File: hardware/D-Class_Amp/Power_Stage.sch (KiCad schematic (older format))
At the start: 18 parts, among them Q501 PHP23NQ11T, Q502 PHP23NQ11T, Q503 PHP23NQ11T, Q504 PHP23NQ11T, U502 IR21834, U503 IR21834

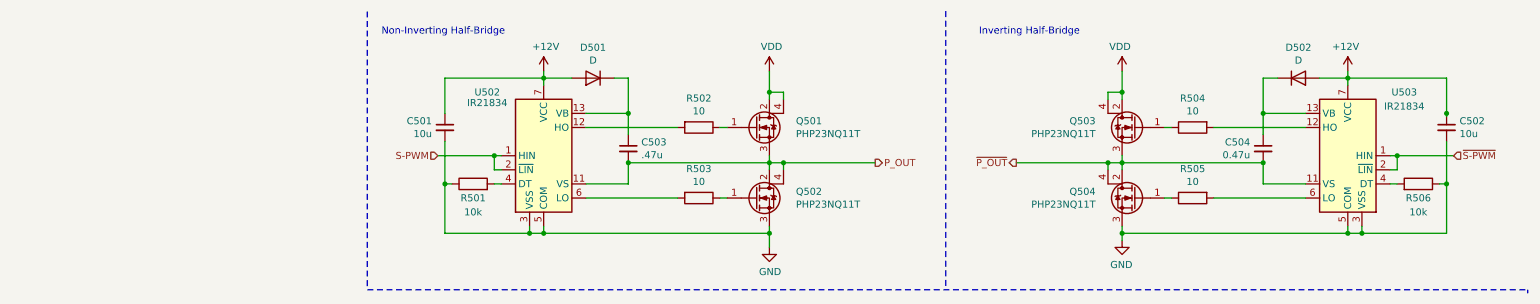
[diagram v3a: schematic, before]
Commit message: updated fet footprints, and added power stage test points
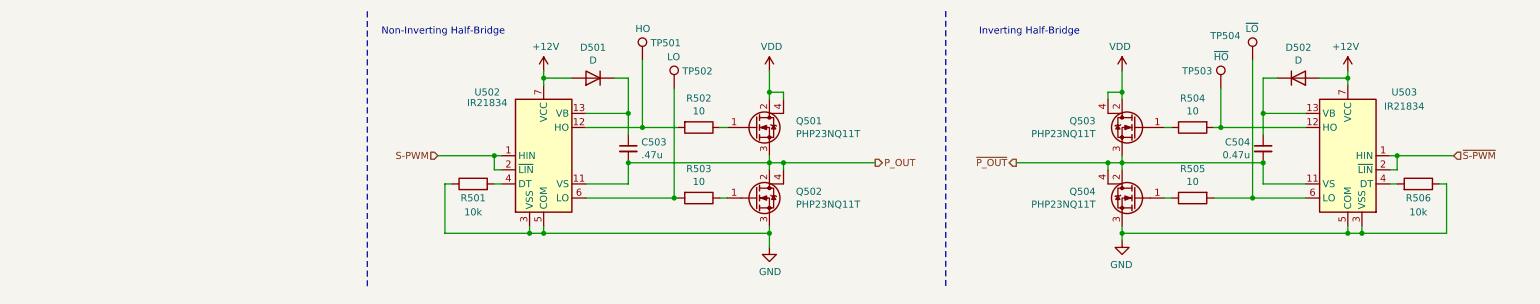
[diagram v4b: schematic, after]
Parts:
- removed C501, C502: 10u, Capacitor_SMD:C_0805_2012Metric_Pad1.18x1.45mm_HandSolder, symbol Device:C_Small
- added TP501: HO, TestPoint:TestPoint_THTPad_D2.0mm_Drill1.0mm, symbol Connector:TestPoint
- added TP502: LO, TestPoint:TestPoint_THTPad_D2.0mm_Drill1.0mm, symbol Connector:TestPoint
- added TP503: ~HO, TestPoint:TestPoint_THTPad_D2.0mm_Drill1.0mm, symbol Connector:TestPoint
- added TP504: ~LO, TestPoint:TestPoint_THTPad_D2.0mm_Drill1.0mm, symbol Connector:TestPoint
- Q502, Q503, Q504: footprint Package_TO_SOT_THT:TO-251-3-1EP_Horizontal_TabD -> Package_TO_SOT_THT:TO-251-3-1EP_Horizontal_TabDown
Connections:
- net at R502.2, U502.12 (HO): now also TP501.1
- net at R503.2, U502.6 (LO): now also TP502.1
- net at R504.2, U503.12 (HO): now also TP503.1
- net at R505.2, U503.6 (LO): now also TP504.1
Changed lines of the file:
@@
 Connection ~ 5950 1550
 Wire Wire Line
-	4550 1300 5200 1300
-Wire Wire Line
-	4550 1800 5200 1800
+	4550 1300 4950 1300
 Wire Wire Line
 	5850 1550 4850 1550
@@
 $EndComp
 $Comp
-L Device:Q_NMOS_GDSD Q502
-U 1 1 6104F394
-P 5750 1800
-F 0 "Q502" H 6038 1846 50  0000 L CNN
-F 1 "PHP23NQ11T" H 6038 1755 50  0000 L CNN
-F 2 "Package_TO_SOT_THT:TO-251-3-1EP_Horizontal_TabD" H 5950 1900 50  0001 C CNN
-F 3 "https://assets.nexperia.com/documents/data-sheet/PHP23NQ11T.pdf" H 5750 1800 50  0001 C CNN
-	1    5750 1800
-	1    0    0    -1
-$EndComp
-$Comp
 L Device:Q_NMOS_GDSD Q501
 U 1 1 6104F024
@@
 $EndComp
 $Comp
-L Device:Q_NMOS_GDSD Q503
-U 1 1 610F221C
-P 8450 1300
-F 0 "Q503" H 8738 1346 50  0000 L CNN
-F 1 "PHP23NQ11T" H 8738 1255 50  0000 L CNN
-F 2 "Package_TO_SOT_THT:TO-251-3-1EP_Horizontal_TabD" H 8650 1400 50  0001 C CNN
-F 3 "https://assets.nexperia.com/documents/data-sheet/PHP23NQ11T.pdf" H 8450 1300 50  0001 C CNN
-	1    8450 1300
-	-1   0    0    -1
-$EndComp
-$Comp
-L Device:Q_NMOS_GDSD Q504
-U 1 1 610F2226
-P 8450 1800
-F 0 "Q504" H 8738 1846 50  0000 L CNN
-F 1 "PHP23NQ11T" H 8738 1755 50  0000 L CNN
-F 2 "Package_TO_SOT_THT:TO-251-3-1EP_Horizontal_TabD" H 8650 1900 50  0001 C CNN
-F 3 "https://assets.nexperia.com/documents/data-sheet/PHP23NQ11T.pdf" H 8450 1800 50  0001 C CNN
-	1    8450 1800
-	-1   0    0    -1
-$EndComp
-$Comp
 L Driver_FET:IR21834 U503
 U 1 1 610F2212
@@
 	8350 1550 9350 1550
 Wire Wire Line
-	9650 1800 9000 1800
-Wire Wire Line
-	9650 1300 9000 1300
+	9650 1800 9275 1800
+Wire Wire Line
+	9650 1300 9050 1300
 Connection ~ 8250 1550
 Wire Wire Line
@@
 	8350 1100 8350 1050
 Connection ~ 8350 1550
-Wire Wire Line
-	8350 1550 8350 1500
 Wire Wire Line
 	8350 1550 8350 1600
@@
 $EndComp
 $Comp
-L Device:C_Small C501
-U 1 1 61139FFD
-P 3550 1300
-F 0 "C501" H 3642 1346 50  0000 L CNN
-F 1 "10u" H 3642 1255 50  0000 L CNN
-F 2 "Capacitor_SMD:C_0805_2012Metric_Pad1.18x1.45mm_HandSolder" H 3550 1300 50  0001 C CNN
-F 3 "~" H 3550 1300 50  0001 C CNN
-	1    3550 1300
-	-1   0    0    -1
-$EndComp
-$Comp
-L Device:C_Small C502
-U 1 1 6113D2CB
-P 10650 1300
-F 0 "C502" H 10742 1346 50  0000 L CNN
-F 1 "10u" H 10742 1255 50  0000 L CNN
-F 2 "Capacitor_SMD:C_0805_2012Metric_Pad1.18x1.45mm_HandSolder" H 10650 1300 50  0001 C CNN
-F 3 "~" H 10650 1300 50  0001 C CNN
-	1    10650 1300
-	1    0    0    -1
-$EndComp
-Wire Wire Line
-	10650 1700 10650 1400
-Connection ~ 10650 1700
-Wire Wire Line
-	10650 1225 10650 1200
-Connection ~ 10650 1200
-Wire Wire Line
-	10650 1200 10650 950
-Wire Wire Line
-	9950 950  10650 950
-Wire Wire Line
-	3550 1700 3550 1400
-Connection ~ 3550 1700
-Wire Wire Line
-	3550 1200 3550 950
-Wire Wire Line
-	3550 950  4250 950
-Wire Notes Line
-	3000 2450 11225 2450
-Wire Notes Line
-	11225 2450 11225 2475
+L Connector:TestPoint TP?
+U 1 1 61148EFA
+P 4950 825
+AR Path="/61148EFA" Ref="TP?"  Part="1"
+AR Path="/610497A4/61148EFA" Ref="TP501"  Part="1"
+F 0 "TP501" H 5008 949 50  0000 L CNN
+F 1 "HO" H 4900 1050 50  0000 L CNN
+F 2 "TestPoint:TestPoint_THTPad_D2.0mm_Drill1.0mm" H 5150 825 50  0001 C CNN
+F 3 "~" H 5150 825 50  0001 C CNN
+	1    4950 825
+	1    0    0    -1
+$EndComp
+$Comp
+L Connector:TestPoint TP?
+U 1 1 6114A61F
+P 5175 1025
+AR Path="/6114A61F" Ref="TP?"  Part="1"
+AR Path="/610497A4/6114A61F" Ref="TP502"  Part="1"
+F 0 "TP502" H 5233 1149 50  0000 L CNN
+F 1 "LO" H 5125 1250 50  0000 L CNN
+F 2 "TestPoint:TestPoint_THTPad_D2.0mm_Drill1.0mm" H 5375 1025 50  0001 C CNN
+F 3 "~" H 5375 1025 50  0001 C CNN
+	1    5175 1025
+	1    0    0    -1
+$EndComp
+Wire Wire Line
+	4950 825  4950 1300
+Connection ~ 4950 1300
+Wire Wire Line
+	4950 1300 5200 1300
+Wire Wire Line
+	4550 1800 5175 1800
+Connection ~ 5175 1800
+Wire Wire Line
+	5175 1800 5200 1800
+Wire Wire Line
+	5175 1025 5175 1800
+$Comp
+L Connector:TestPoint TP?
+U 1 1 61152F83
+P 9050 1025
+AR Path="/61152F83" Ref="TP?"  Part="1"
+AR Path="/610497A4/61152F83" Ref="TP503"  Part="1"
+F 0 "TP503" H 8775 1150 50  0000 L CNN
+F 1 "~HO" H 9000 1250 50  0000 L CNN
+F 2 "TestPoint:TestPoint_THTPad_D2.0mm_Drill1.0mm" H 9250 1025 50  0001 C CNN
+F 3 "~" H 9250 1025 50  0001 C CNN
+	1    9050 1025
+	1    0    0    -1
+$EndComp
+$Comp
+L Connector:TestPoint TP?
+U 1 1 61153163
+P 9275 825
+AR Path="/61153163" Ref="TP?"  Part="1"
+AR Path="/610497A4/61153163" Ref="TP504"  Part="1"
+F 0 "TP504" H 8975 1000 50  0000 L CNN
+F 1 "~LO" H 9225 1050 50  0000 L CNN
+F 2 "TestPoint:TestPoint_THTPad_D2.0mm_Drill1.0mm" H 9475 825 50  0001 C CNN
+F 3 "~" H 9475 825 50  0001 C CNN
+	1    9275 825
+	1    0    0    -1
+$EndComp
+Wire Wire Line
+	9050 1025 9050 1300
+Wire Wire Line
+	9275 825  9275 1800
+Connection ~ 9050 1300
+Wire Wire Line
+	9050 1300 9000 1300
+Connection ~ 9275 1800
+Wire Wire Line
+	9275 1800 9000 1800
+$Comp
+L Device:Q_NMOS_GDSD Q502
+U 1 1 61187A5E
+P 5750 1800
+F 0 "Q502" H 6038 1846 50  0000 L CNN
+F 1 "PHP23NQ11T" H 6038 1755 50  0000 L CNN
+F 2 "Package_TO_SOT_THT:TO-251-3-1EP_Horizontal_TabDown" H 5950 1900 50  0001 C CNN
+F 3 "https://assets.nexperia.com/documents/data-sheet/PHP23NQ11T.pdf" H 5750 1800 50  0001 C CNN
+	1    5750 1800
+	1    0    0    -1
+$EndComp
+Wire Wire Line
+	8350 1550 8350 1500
+$Comp
+L Device:Q_NMOS_GDSD Q503
+U 1 1 6118B010
+P 8450 1300
+F 0 "Q503" H 8738 1346 50  0000 L CNN
+F 1 "PHP23NQ11T" H 8738 1255 50  0000 L CNN
+F 2 "Package_TO_SOT_THT:TO-251-3-1EP_Horizontal_TabDown" H 8650 1400 50  0001 C CNN
+F 3 "https://assets.nexperia.com/documents/data-sheet/PHP23NQ11T.pdf" H 8450 1300 50  0001 C CNN
+	1    8450 1300
+	-1   0    0    -1
+$EndComp
+$Comp
+L Device:Q_NMOS_GDSD Q504
+U 1 1 6118BB1D
+P 8450 1800
+F 0 "Q504" H 8738 1846 50  0000 L CNN
+F 1 "PHP23NQ11T" H 8738 1755 50  0000 L CNN
+F 2 "Package_TO_SOT_THT:TO-251-3-1EP_Horizontal_TabDown" H 8650 1900 50  0001 C CNN
+F 3 "https://assets.nexperia.com/documents/data-sheet/PHP23NQ11T.pdf" H 8450 1800 50  0001 C CNN
+	1    8450 1800
+	-1   0    0    -1
+$EndComp
 $EndSCHEMATC

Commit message: re-added supply caps for the gate driver
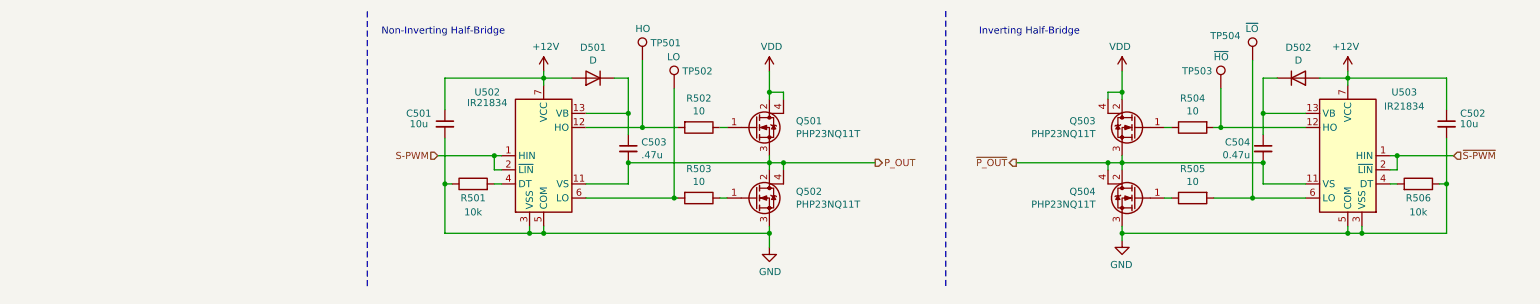
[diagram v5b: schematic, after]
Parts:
- added C501, C502: 10u, Capacitor_SMD:C_0805_2012Metric_Pad1.18x1.45mm_HandSolder, symbol Device:C_Small
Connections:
- net +12V: now also C501.1, C502.1
- net GND: now also C501.2, C502.2
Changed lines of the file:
@@
 	-1   0    0    -1
 $EndComp
+$Comp
+L Device:C_Small C501
+U 1 1 61199493
+P 3550 1275
+F 0 "C501" H 3275 1350 50  0000 L CNN
+F 1 "10u" H 3300 1275 50  0000 L CNN
+F 2 "Capacitor_SMD:C_0805_2012Metric_Pad1.18x1.45mm_HandSolder" H 3550 1275 50  0001 C CNN
+F 3 "~" H 3550 1275 50  0001 C CNN
+	1    3550 1275
+	1    0    0    -1
+$EndComp
+$Comp
+L Device:C_Small C502
+U 1 1 6119B46C
+P 10650 1275
+F 0 "C502" H 10375 1350 50  0000 L CNN
+F 1 "10u" H 10425 1275 50  0000 L CNN
+F 2 "Capacitor_SMD:C_0805_2012Metric_Pad1.18x1.45mm_HandSolder" H 10650 1275 50  0001 C CNN
+F 3 "~" H 10650 1275 50  0001 C CNN
+	1    10650 1275
+	-1   0    0    -1
+$EndComp
+Wire Wire Line
+	10650 1700 10650 1375
+Connection ~ 10650 1700
+Wire Wire Line
+	10650 1175 10650 950
+Wire Wire Line
+	10650 950  9950 950
+Wire Wire Line
+	4250 950  3550 950
+Wire Wire Line
+	3550 950  3550 1175
+Wire Wire Line
+	3550 1375 3550 1700
+Connection ~ 3550 1700
 $EndSCHEMATC

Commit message: Add footprints to the output filter and select output filter components
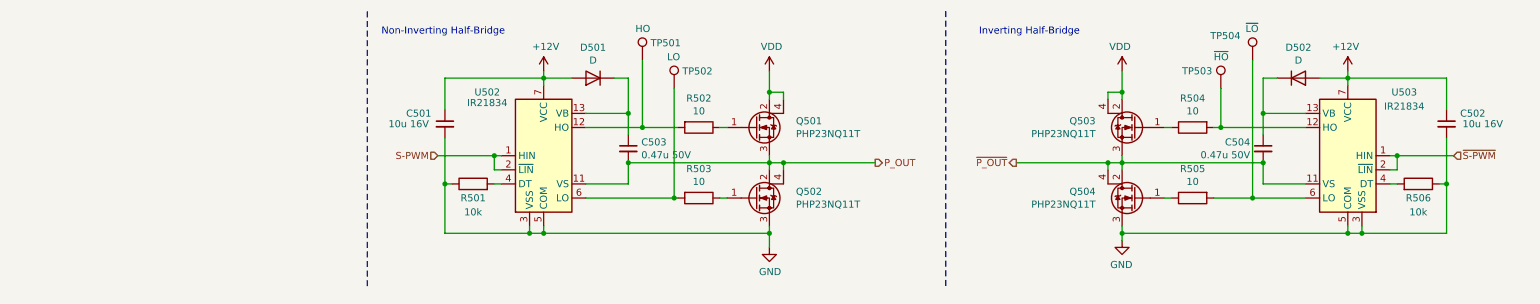
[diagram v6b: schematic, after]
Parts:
- C501, C502: value 10u -> 10u 16V
- C503: value .47u -> 0.47u 50V
- C504: value 0.47u -> 0.47u 50V
- U502, U503: Digikey IR21834SPBFDKR-ND -> (none); Part Number (none) -> IR21834SPBFDKR-ND
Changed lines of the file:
@@
 P 4850 1450
 F 0 "C503" H 4942 1496 50  0000 L CNN
-F 1 ".47u" H 4942 1405 50  0000 L CNN
+F 1 "0.47u 50V" H 4942 1405 50  0000 L CNN
 F 2 "Capacitor_SMD:C_0805_2012Metric_Pad1.18x1.45mm_HandSolder" H 4850 1450 50  0001 C CNN
 F 3 "~" H 4850 1450 50  0001 C CNN
@@
 F 2 "Package_SO:SOIC-14_3.9x8.7mm_P1.27mm" H 4250 1500 50  0001 C CIN
 F 3 "https://www.infineon.com/dgdl/ir2183.pdf?fileId=5546d462533600a4015355c9490e16d1" H 4250 1500 50  0001 C CNN
-F 4 "IR21834SPBFDKR-ND" H 4250 1500 50  0001 C CNN "Digikey"
+F 4 "IR21834SPBFDKR-ND" H 4250 1500 50  0001 C CNN "Part Number"
 	1    4250 1500
 	1    0    0    -1
@@
 F 2 "Package_SO:SOIC-14_3.9x8.7mm_P1.27mm" H 9950 1500 50  0001 C CIN
 F 3 "https://www.infineon.com/dgdl/ir2183.pdf?fileId=5546d462533600a4015355c9490e16d1" H 9950 1500 50  0001 C CNN
-F 4 "IR21834SPBFDKR-ND" H 9950 1500 50  0001 C CNN "Digikey"
+F 4 "IR21834SPBFDKR-ND" H 9950 1500 50  0001 C CNN "Part Number"
 	1    9950 1500
 	-1   0    0    -1
@@
 P 9350 1450
 F 0 "C504" H 9442 1496 50  0000 L CNN
-F 1 "0.47u" H 9442 1405 50  0000 L CNN
+F 1 "0.47u 50V" H 9442 1405 50  0000 L CNN
 F 2 "Capacitor_SMD:C_0805_2012Metric_Pad1.18x1.45mm_HandSolder" H 9350 1450 50  0001 C CNN
 F 3 "~" H 9350 1450 50  0001 C CNN
@@
 P 3550 1275
 F 0 "C501" H 3275 1350 50  0000 L CNN
-F 1 "10u" H 3300 1275 50  0000 L CNN
+F 1 "10u 16V" H 3150 1275 50  0000 L CNN
 F 2 "Capacitor_SMD:C_0805_2012Metric_Pad1.18x1.45mm_HandSolder" H 3550 1275 50  0001 C CNN
 F 3 "~" H 3550 1275 50  0001 C CNN
@@
 P 10650 1275
 F 0 "C502" H 10375 1350 50  0000 L CNN
-F 1 "10u" H 10425 1275 50  0000 L CNN
+F 1 "10u 16V" H 10250 1275 50  0000 L CNN
 F 2 "Capacitor_SMD:C_0805_2012Metric_Pad1.18x1.45mm_HandSolder" H 10650 1275 50  0001 C CNN
 F 3 "~" H 10650 1275 50  0001 C CNN
